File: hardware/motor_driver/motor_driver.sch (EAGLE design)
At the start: 79 parts

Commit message: Added temperature sensor
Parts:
- added C27: 2.2u, adafruit:C-USC0805
- added R32: 10K, adafruit:R-US_M0805
- added TEMP: 22-23-2021, con-molex:22-23-2021
- added U$11: NCP18XH103F03RB, bldc_lib:NCP18XH103F03RB
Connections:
- new net TEMP: C27.1, R32.1, TEMP-2.S, U$11.1
- net +3V3: now also U$11.2
- net DGND: now also C27.2, R32.2, TEMP-1.S
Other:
- note added: "NTC 10K"
- note added: "Temperature Sensor"
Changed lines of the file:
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@@
 <setting verticaltext="up"/>
 </settings>
-<grid distance="0.1" unitdist="inch" unit="inch" style="lines" multiple="1" display="yes" altdistance="0.01" altunitdist="inch" altunit="inch"/>
+<grid distance="0.1" unitdist="inch" unit="inch" style="lines" multiple="1" display="no" altdistance="0.01" altunitdist="inch" altunit="inch"/>
 <layers>
 <layer number="1" name="Top" color="4" fill="1" visible="no" active="no"/>
@@
 <part name="PT1" library="SparkFun-Passives" deviceset="2PT_GND_TIE" device=""/>
 <part name="PT2" library="SparkFun-Passives" deviceset="2PT_GND_TIE" device=""/>
+<part name="U$11" library="bldc_lib" deviceset="NCP18XH103F03RB" device=""/>
+<part name="R32" library="adafruit" deviceset="R-US_" device="M0805" value="10K"/>
+<part name="SUPPLY24" library="supply2" deviceset="DGND" device=""/>
+<part name="+3V2" library="supply1" deviceset="+3V3" device=""/>
+<part name="C27" library="adafruit" deviceset="C-US" device="C0805" value="2.2u"/>
+<part name="TEMP" library="con-molex" deviceset="22-23-2021" device=""/>
 </parts>
 <sheets>
@@
 <wire x1="88.9" y1="-66.04" x2="124.46" y2="-66.04" width="0.1524" layer="97" style="shortdash"/>
 <text x="96.52" y="-63.5" size="2.54" layer="97">Connect Grounds</text>
+<text x="7.62" y="-50.8" size="1.778" layer="97">NTC 10K</text>
+<wire x1="55.88" y1="-22.86" x2="55.88" y2="-53.34" width="0.1524" layer="97" style="shortdash"/>
+<wire x1="55.88" y1="-53.34" x2="-5.08" y2="-53.34" width="0.1524" layer="97" style="shortdash"/>
+<wire x1="-5.08" y1="-53.34" x2="-5.08" y2="-22.86" width="0.1524" layer="97" style="shortdash"/>
+<wire x1="-5.08" y1="-22.86" x2="55.88" y2="-22.86" width="0.1524" layer="97" style="shortdash"/>
+<text x="30.48" y="-50.8" size="1.778" layer="97">Temperature Sensor</text>
 </plain>
 <instances>
@@
 <instance part="PT1" gate="G$1" x="99.06" y="-86.36"/>
 <instance part="PT2" gate="G$1" x="114.3" y="-86.36"/>
+<instance part="U$11" gate="G$1" x="10.16" y="-40.64"/>
+<instance part="R32" gate="G$1" x="25.4" y="-40.64"/>
+<instance part="SUPPLY24" gate="G$1" x="33.02" y="-40.64" rot="R90"/>
+<instance part="+3V2" gate="G$1" x="0" y="-40.64" rot="R90"/>
+<instance part="C27" gate="G$1" x="22.86" y="-33.02" rot="R90"/>
+<instance part="TEMP" gate="-1" x="45.72" y="-35.56" rot="R270"/>
+<instance part="TEMP" gate="-2" x="43.18" y="-35.56" rot="R270"/>
 </instances>
 <busses>
@@
 <label x="104.14" y="-83.82" size="2.54" layer="95" rot="R90" xref="yes"/>
 </segment>
+<segment>
+<pinref part="R32" gate="G$1" pin="2"/>
+<pinref part="SUPPLY24" gate="G$1" pin="DGND"/>
+<pinref part="C27" gate="G$1" pin="2"/>
+<wire x1="27.94" y1="-33.02" x2="30.48" y2="-33.02" width="0.1524" layer="91"/>
+<wire x1="30.48" y1="-33.02" x2="30.48" y2="-40.64" width="0.1524" layer="91"/>
+<junction x="30.48" y="-40.64"/>
+</segment>
+<segment>
+<pinref part="TEMP" gate="-1" pin="S"/>
+<wire x1="45.72" y1="-33.02" x2="45.72" y2="-30.48" width="0.1524" layer="91"/>
+<label x="45.72" y="-30.48" size="1.016" layer="95" rot="R90" xref="yes"/>
+</segment>
 </net>
 <net name="+5V" class="0">
@@
 <junction x="99.06" y="-33.02"/>
 </segment>
-</net>
+<segment>
+<pinref part="+3V2" gate="G$1" pin="+3V3"/>
+<pinref part="U$11" gate="G$1" pin="2"/>
+<wire x1="2.54" y1="-40.64" x2="5.08" y2="-40.64" width="0.1524" layer="91"/>
+</segment>
+</net>
+<net name="TEMP" class="0">
+<segment>
+<pinref part="U$11" gate="G$1" pin="1"/>
+<pinref part="R32" gate="G$1" pin="1"/>
+<wire x1="15.24" y1="-40.64" x2="17.78" y2="-40.64" width="0.1524" layer="91"/>
+<pinref part="C27" gate="G$1" pin="1"/>
+<wire x1="17.78" y1="-40.64" x2="20.32" y2="-40.64" width="0.1524" layer="91"/>
+<wire x1="20.32" y1="-33.02" x2="17.78" y2="-33.02" width="0.1524" layer="91"/>
+<wire x1="17.78" y1="-33.02" x2="17.78" y2="-40.64" width="0.1524" layer="91"/>
+<junction x="17.78" y="-40.64"/>
+<label x="17.78" y="-33.02" size="1.778" layer="95" rot="R90" xref="yes"/>
+</segment>
+<segment>
+<pinref part="TEMP" gate="-2" pin="S"/>
+<wire x1="43.18" y1="-33.02" x2="43.18" y2="-30.48" width="0.1524" layer="91"/>
+<label x="43.18" y="-30.48" size="1.016" layer="95" rot="R90" xref="yes"/>
+</segment>
+</net>

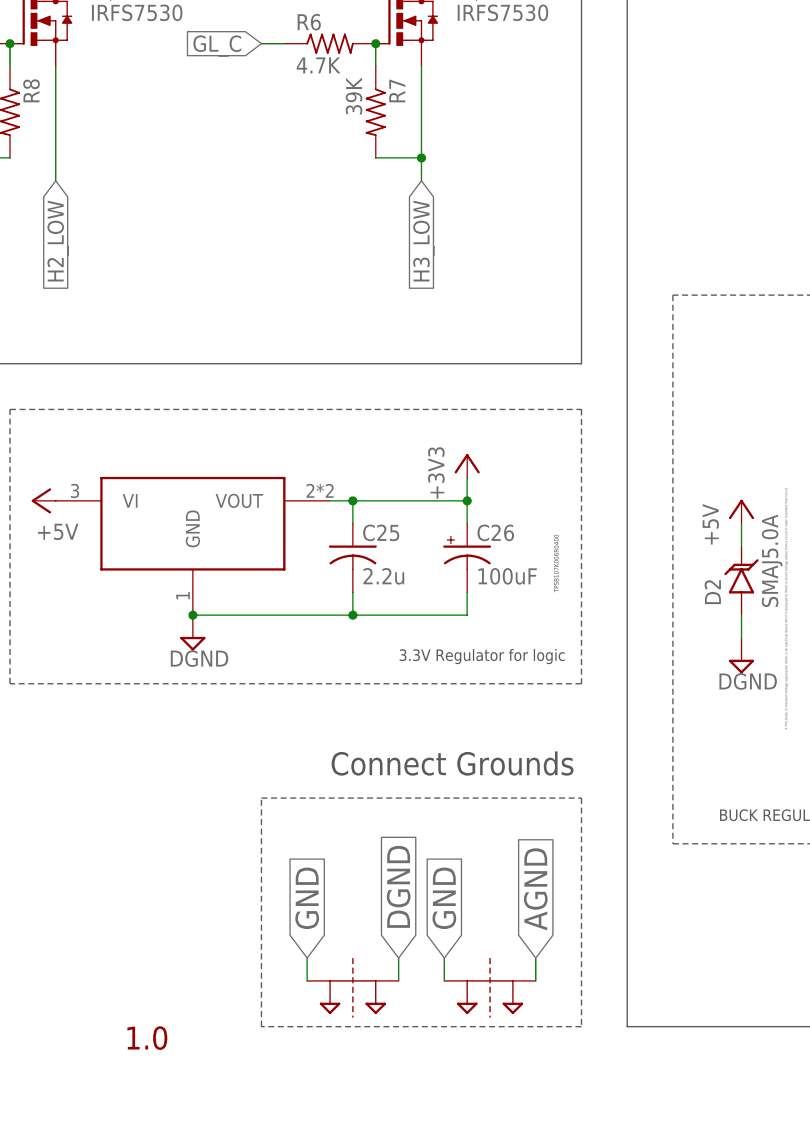
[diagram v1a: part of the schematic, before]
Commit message: Added connectors for motor and power
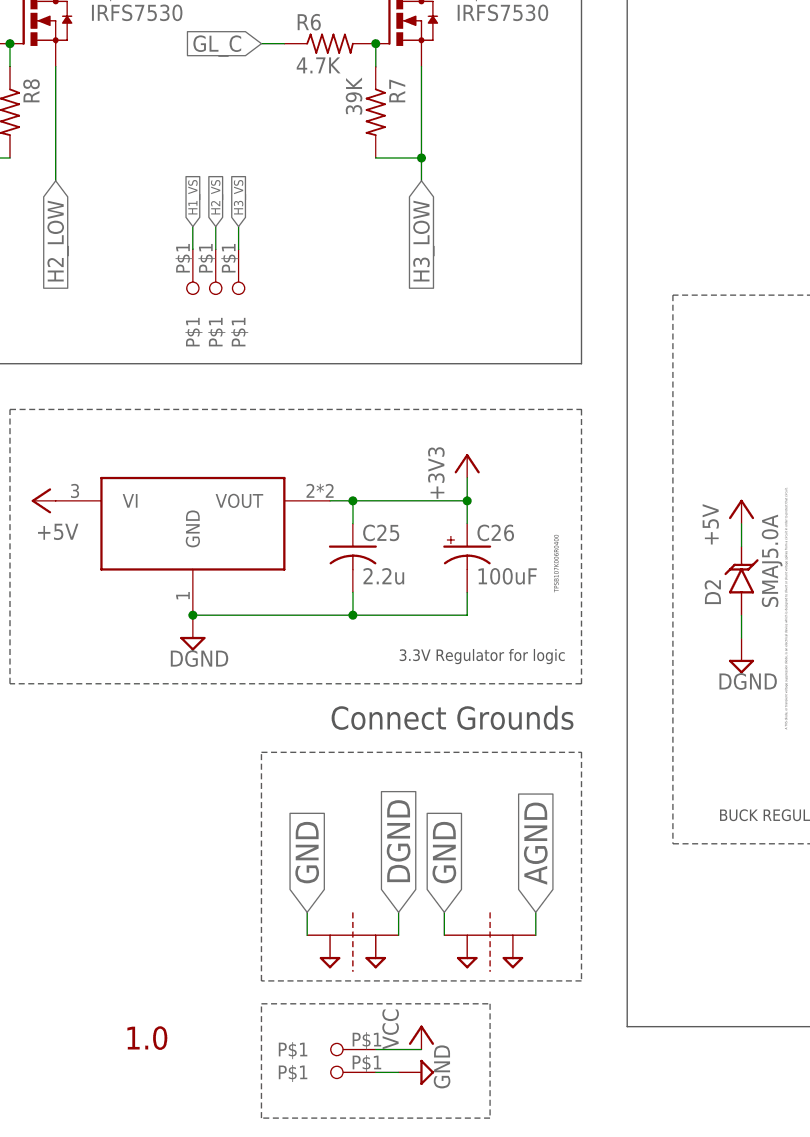
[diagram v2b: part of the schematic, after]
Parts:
- added U$12, U$13, U$14, U$15, U$16: 1CONN_SOLDER, bldc_lib:1CONN_SOLDER
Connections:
- net GND: now also U$16.P$1
- net H1_VS: now also U$14.P$1
- net H2_VS: now also U$13.P$1
- net H3_VS: now also U$12.P$1
- net VCC: now also U$15.P$1
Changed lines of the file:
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@@
 <part name="C27" library="adafruit" deviceset="C-US" device="C0805" value="2.2u"/>
 <part name="TEMP" library="con-molex" deviceset="22-23-2021" device=""/>
+<part name="U$12" library="bldc_lib" deviceset="1CONN_SOLDER" device=""/>
+<part name="U$13" library="bldc_lib" deviceset="1CONN_SOLDER" device=""/>
+<part name="U$14" library="bldc_lib" deviceset="1CONN_SOLDER" device=""/>
+<part name="U$15" library="bldc_lib" deviceset="1CONN_SOLDER" device=""/>
+<part name="U$16" library="bldc_lib" deviceset="1CONN_SOLDER" device=""/>
+<part name="P+14" library="supply1" deviceset="VCC" device=""/>
+<part name="SUPPLY25" library="supply2" deviceset="GND" device=""/>
 </parts>
 <sheets>
@@
 <text x="27.94" y="-83.82" size="2.54" layer="94">Motor Driver (2015)</text>
 <text x="73.66" y="-93.98" size="2.54" layer="94">1.0</text>
-<wire x1="124.46" y1="-66.04" x2="124.46" y2="-91.44" width="0.1524" layer="97" style="shortdash"/>
-<wire x1="124.46" y1="-91.44" x2="88.9" y2="-91.44" width="0.1524" layer="97" style="shortdash"/>
-<wire x1="88.9" y1="-91.44" x2="88.9" y2="-66.04" width="0.1524" layer="97" style="shortdash"/>
-<wire x1="88.9" y1="-66.04" x2="124.46" y2="-66.04" width="0.1524" layer="97" style="shortdash"/>
-<text x="96.52" y="-63.5" size="2.54" layer="97">Connect Grounds</text>
+<wire x1="124.46" y1="-60.96" x2="124.46" y2="-86.36" width="0.1524" layer="97" style="shortdash"/>
+<wire x1="124.46" y1="-86.36" x2="88.9" y2="-86.36" width="0.1524" layer="97" style="shortdash"/>
+<wire x1="88.9" y1="-86.36" x2="88.9" y2="-60.96" width="0.1524" layer="97" style="shortdash"/>
+<wire x1="88.9" y1="-60.96" x2="124.46" y2="-60.96" width="0.1524" layer="97" style="shortdash"/>
+<text x="96.52" y="-58.42" size="2.54" layer="97">Connect Grounds</text>
 <text x="7.62" y="-50.8" size="1.778" layer="97">NTC 10K</text>
 <wire x1="55.88" y1="-22.86" x2="55.88" y2="-53.34" width="0.1524" layer="97" style="shortdash"/>
@@
 <wire x1="-5.08" y1="-22.86" x2="55.88" y2="-22.86" width="0.1524" layer="97" style="shortdash"/>
 <text x="30.48" y="-50.8" size="1.778" layer="97">Temperature Sensor</text>
+<wire x1="88.9" y1="-88.9" x2="114.3" y2="-88.9" width="0.1524" layer="97" style="shortdash"/>
+<wire x1="114.3" y1="-88.9" x2="114.3" y2="-101.6" width="0.1524" layer="97" style="shortdash"/>
+<wire x1="114.3" y1="-101.6" x2="88.9" y2="-101.6" width="0.1524" layer="97" style="shortdash"/>
+<wire x1="88.9" y1="-101.6" x2="88.9" y2="-88.9" width="0.1524" layer="97" style="shortdash"/>
 </plain>
 <instances>
@@
 <instance part="FRAME1" gate="G$1" x="-15.24" y="-101.6"/>
 <instance part="P+1" gate="VCC" x="66.04" y="53.34"/>
-<instance part="PT1" gate="G$1" x="99.06" y="-86.36"/>
-<instance part="PT2" gate="G$1" x="114.3" y="-86.36"/>
+<instance part="PT1" gate="G$1" x="99.06" y="-81.28"/>
+<instance part="PT2" gate="G$1" x="114.3" y="-81.28"/>
 <instance part="U$11" gate="G$1" x="10.16" y="-40.64"/>
 <instance part="R32" gate="G$1" x="25.4" y="-40.64"/>
@@
 <instance part="TEMP" gate="-1" x="45.72" y="-35.56" rot="R270"/>
 <instance part="TEMP" gate="-2" x="43.18" y="-35.56" rot="R270"/>
+<instance part="U$12" gate="G$1" x="86.36" y="-7.62" rot="R270"/>
+<instance part="U$13" gate="G$1" x="83.82" y="-7.62" rot="R270"/>
+<instance part="U$14" gate="G$1" x="81.28" y="-7.62" rot="R270"/>
+<instance part="U$15" gate="G$1" x="99.06" y="-93.98" rot="R180"/>
+<instance part="U$16" gate="G$1" x="99.06" y="-96.52" rot="R180"/>
+<instance part="P+14" gate="VCC" x="106.68" y="-91.44"/>
+<instance part="SUPPLY25" gate="GND" x="106.68" y="-96.52" rot="R90"/>
 </instances>
 <busses>
@@
 <label x="327.66" y="-33.02" size="1.016" layer="95" rot="R180" xref="yes"/>
 </segment>
+<segment>
+<pinref part="U$14" gate="G$1" pin="P$1"/>
+<wire x1="81.28" y1="-5.08" x2="81.28" y2="-2.54" width="0.1524" layer="91"/>
+<label x="81.28" y="-2.54" size="1.016" layer="95" rot="R90" xref="yes"/>
+</segment>
 </net>
 <net name="H2_VS" class="0">
@@
 <label x="327.66" y="-50.8" size="1.016" layer="95" rot="R180" xref="yes"/>
 </segment>
+<segment>
+<pinref part="U$13" gate="G$1" pin="P$1"/>
+<wire x1="83.82" y1="-5.08" x2="83.82" y2="-2.54" width="0.1524" layer="91"/>
+<label x="83.82" y="-2.54" size="1.016" layer="95" rot="R90" xref="yes"/>
+</segment>
 </net>
 <net name="H3_VS" class="0">
@@
 <wire x1="330.2" y1="-68.58" x2="327.66" y2="-68.58" width="0.1524" layer="91"/>
 <label x="327.66" y="-68.58" size="1.016" layer="95" rot="R180" xref="yes"/>
+</segment>
+<segment>
+<pinref part="U$12" gate="G$1" pin="P$1"/>
+<wire x1="86.36" y1="-5.08" x2="86.36" y2="-2.54" width="0.1524" layer="91"/>
+<label x="86.36" y="-2.54" size="1.016" layer="95" rot="R90" xref="yes"/>
 </segment>
 </net>
@@
 </segment>
 <segment>
-<wire x1="93.98" y1="-86.36" x2="93.98" y2="-83.82" width="0.1524" layer="91"/>
-<label x="93.98" y="-83.82" size="2.54" layer="95" rot="R90" xref="yes"/>
+<wire x1="93.98" y1="-81.28" x2="93.98" y2="-78.74" width="0.1524" layer="91"/>
+<label x="93.98" y="-78.74" size="2.54" layer="95" rot="R90" xref="yes"/>
 <pinref part="PT1" gate="G$1" pin="P$1"/>
 </segment>
 <segment>
 <pinref part="PT2" gate="G$1" pin="P$1"/>
-<wire x1="109.22" y1="-86.36" x2="109.22" y2="-83.82" width="0.1524" layer="91"/>
-<label x="109.22" y="-83.82" size="2.54" layer="95" rot="R90" xref="yes"/>
+<wire x1="109.22" y1="-81.28" x2="109.22" y2="-78.74" width="0.1524" layer="91"/>
+<label x="109.22" y="-78.74" size="2.54" layer="95" rot="R90" xref="yes"/>
+</segment>
+<segment>
+<pinref part="U$16" gate="G$1" pin="P$1"/>
+<wire x1="101.6" y1="-96.52" x2="104.14" y2="-96.52" width="0.1524" layer="91"/>
+<pinref part="SUPPLY25" gate="GND" pin="GND"/>
 </segment>
 </net>
@@
 <segment>
 <pinref part="PT2" gate="G$1" pin="P$2"/>
-<wire x1="119.38" y1="-86.36" x2="119.38" y2="-83.82" width="0.1524" layer="91"/>
-<label x="119.38" y="-83.82" size="2.54" layer="95" rot="R90" xref="yes"/>
+<wire x1="119.38" y1="-81.28" x2="119.38" y2="-78.74" width="0.1524" layer="91"/>
+<label x="119.38" y="-78.74" size="2.54" layer="95" rot="R90" xref="yes"/>
 </segment>
 </net>
@@
 <segment>
 <pinref part="PT1" gate="G$1" pin="P$2"/>
-<wire x1="104.14" y1="-86.36" x2="104.14" y2="-83.82" width="0.1524" layer="91"/>
-<label x="104.14" y="-83.82" size="2.54" layer="95" rot="R90" xref="yes"/>
+<wire x1="104.14" y1="-81.28" x2="104.14" y2="-78.74" width="0.1524" layer="91"/>
+<label x="104.14" y="-78.74" size="2.54" layer="95" rot="R90" xref="yes"/>
 </segment>
 <segment>
@@
 <wire x1="66.04" y1="48.26" x2="66.04" y2="50.8" width="0.1524" layer="91"/>
 </segment>
-</net>
+<segment>
+<pinref part="U$15" gate="G$1" pin="P$1"/>
+<wire x1="101.6" y1="-93.98" x2="106.68" y2="-93.98" width="0.1524" layer="91"/>
+<pinref part="P+14" gate="VCC" pin="VCC"/>
+</segment>
+</net>

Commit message: Grounded MOSFETS
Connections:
- removed net H2_LOW: U$3.S, U$7.SL_B
- removed net N$25: R10.2, U$8.2
- removed net N$9: R12.2, U$9.2
- net GND: now also U$3.S, U$7.SL_B
- net H1_LOW: now also R10.2, U$8.2
- net H3_LOW: now also R12.2, U$9.2
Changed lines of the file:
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@@
 <part name="P+14" library="supply1" deviceset="VCC" device=""/>
 <part name="SUPPLY25" library="supply2" deviceset="GND" device=""/>
+<part name="SUPPLY26" library="supply2" deviceset="GND" device=""/>
+<part name="SUPPLY27" library="supply2" deviceset="GND" device=""/>
 </parts>
 <sheets>
@@
 <text x="58.42" y="63.5" size="1.778" layer="97">MOSFET</text>
 <wire x1="238.76" y1="-50.8" x2="238.76" y2="-86.36" width="0.1524" layer="97" style="shortdash"/>
-<wire x1="238.76" y1="-86.36" x2="299.72" y2="-86.36" width="0.1524" layer="97" style="shortdash"/>
-<wire x1="299.72" y1="-86.36" x2="299.72" y2="-25.4" width="0.1524" layer="97" style="shortdash"/>
-<wire x1="299.72" y1="-25.4" x2="276.86" y2="-25.4" width="0.1524" layer="97" style="shortdash"/>
+<wire x1="238.76" y1="-86.36" x2="314.96" y2="-86.36" width="0.1524" layer="97" style="shortdash"/>
+<wire x1="314.96" y1="-86.36" x2="314.96" y2="-25.4" width="0.1524" layer="97" style="shortdash"/>
+<wire x1="314.96" y1="-25.4" x2="276.86" y2="-25.4" width="0.1524" layer="97" style="shortdash"/>
 <wire x1="276.86" y1="-25.4" x2="276.86" y2="-27.94" width="0.1524" layer="97" style="shortdash"/>
 <wire x1="276.86" y1="-27.94" x2="243.84" y2="-27.94" width="0.1524" layer="97" style="shortdash"/>
@@
 <instance part="P+14" gate="VCC" x="106.68" y="-91.44"/>
 <instance part="SUPPLY25" gate="GND" x="106.68" y="-96.52" rot="R90"/>
+<instance part="SUPPLY26" gate="GND" x="66.04" y="7.62"/>
+<instance part="SUPPLY27" gate="GND" x="269.24" y="-12.7" rot="R90"/>
 </instances>
 <busses>
@@
 <label x="264.16" y="0" size="1.016" layer="95" xref="yes"/>
 </segment>
-</net>
-<net name="H2_LOW" class="0">
-<segment>
-<pinref part="U$3" gate="G$1" pin="S"/>
-<wire x1="66.04" y1="15.24" x2="66.04" y2="2.54" width="0.1524" layer="91"/>
-<label x="66.04" y="2.54" size="1.778" layer="95" rot="R270" xref="yes"/>
-</segment>
-<segment>
-<pinref part="U$7" gate="G$1" pin="SL_B"/>
-<wire x1="261.62" y1="-12.7" x2="264.16" y2="-12.7" width="0.1524" layer="91"/>
-<label x="264.16" y="-12.7" size="1.016" layer="95" xref="yes"/>
+<segment>
+<pinref part="R10" gate="G$1" pin="2"/>
+<pinref part="U$8" gate="R$1" pin="2"/>
+<wire x1="292.1" y1="-30.48" x2="294.64" y2="-30.48" width="0.1524" layer="91"/>
+<wire x1="294.64" y1="-30.48" x2="299.72" y2="-30.48" width="0.1524" layer="91"/>
+<junction x="294.64" y="-30.48"/>
+<label x="299.72" y="-30.48" size="1.778" layer="95" xref="yes"/>
 </segment>
 </net>
@@
 <label x="264.16" y="-25.4" size="1.016" layer="95" xref="yes"/>
 </segment>
+<segment>
+<pinref part="U$9" gate="R$1" pin="2"/>
+<pinref part="R12" gate="G$1" pin="2"/>
+<wire x1="294.64" y1="-50.8" x2="292.1" y2="-50.8" width="0.1524" layer="91"/>
+<wire x1="294.64" y1="-50.8" x2="299.72" y2="-50.8" width="0.1524" layer="91"/>
+<junction x="294.64" y="-50.8"/>
+<label x="299.72" y="-50.8" size="1.778" layer="95" xref="yes"/>
+</segment>
 </net>
 <net name="GL_A" class="0">
@@
 <pinref part="C3" gate="G$1" pin="1"/>
 <wire x1="274.32" y1="-15.24" x2="261.62" y2="-15.24" width="0.1524" layer="91"/>
-</segment>
-</net>
-<net name="N$9" class="0">
-<segment>
-<pinref part="U$9" gate="R$1" pin="2"/>
-<pinref part="R12" gate="G$1" pin="2"/>
-<wire x1="294.64" y1="-50.8" x2="292.1" y2="-50.8" width="0.1524" layer="91"/>
 </segment>
 </net>
@@
 <wire x1="271.78" y1="-40.64" x2="276.86" y2="-40.64" width="0.1524" layer="91"/>
 <junction x="276.86" y="-40.64"/>
-</segment>
-</net>
-<net name="N$25" class="0">
-<segment>
-<pinref part="R10" gate="G$1" pin="2"/>
-<pinref part="U$8" gate="R$1" pin="2"/>
-<wire x1="292.1" y1="-30.48" x2="294.64" y2="-30.48" width="0.1524" layer="91"/>
 </segment>
 </net>
@@
 <pinref part="SUPPLY25" gate="GND" pin="GND"/>
 </segment>
-</net>
+<segment>
+<pinref part="U$3" gate="G$1" pin="S"/>
+<wire x1="66.04" y1="15.24" x2="66.04" y2="10.16" width="0.1524" layer="91"/>
+<pinref part="SUPPLY26" gate="GND" pin="GND"/>
+</segment>
+<segment>
+<pinref part="U$7" gate="G$1" pin="SL_B"/>
+<wire x1="261.62" y1="-12.7" x2="266.7" y2="-12.7" width="0.1524" layer="91"/>
+<pinref part="SUPPLY27" gate="GND" pin="GND"/>
+</segment>
+</net>

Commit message: Made the changes mike suggested
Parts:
- R19: value 10M -> 1M
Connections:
- net DGND: now also C11.1
- net GND: no longer C11.1
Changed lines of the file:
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@@
 <part name="R18" library="adafruit" deviceset="R-US_" device="R0603" value="10K"/>
 <part name="SUPPLY7" library="supply2" deviceset="DGND" device=""/>
-<part name="R19" library="adafruit" deviceset="R-US_" device="R0603" value="10M"/>
+<part name="R19" library="adafruit" deviceset="R-US_" device="R0603" value="1M"/>
 <part name="SUPPLY8" library="supply2" deviceset="DGND" device=""/>
 <part name="R20" library="adafruit" deviceset="R-US_" device="R0603" value="15K"/>
@@
 <part name="P+8" library="supply1" deviceset="+5V" device=""/>
 <part name="C11" library="SparkFun-Passives" deviceset="CAP" device="1206" value="10u,50V"/>
-<part name="SUPPLY13" library="supply2" deviceset="GND" device=""/>
 <part name="P+9" library="supply1" deviceset="VCC" device=""/>
 <part name="CTRL" library="con-molex" deviceset="22-23-2041" device=""/>
@@
 <part name="SUPPLY26" library="supply2" deviceset="GND" device=""/>
 <part name="SUPPLY27" library="supply2" deviceset="GND" device=""/>
+<part name="SUPPLY13" library="supply2" deviceset="DGND" device=""/>
 </parts>
 <sheets>
@@
 <instance part="P+8" gate="1" x="142.24" y="-33.02"/>
 <instance part="C11" gate="G$1" x="208.28" y="-20.32" rot="R90"/>
-<instance part="SUPPLY13" gate="GND" x="200.66" y="-17.78" rot="R180"/>
 <instance part="P+9" gate="VCC" x="218.44" y="-15.24"/>
 <instance part="CTRL" gate="-1" x="200.66" y="43.18" rot="R270"/>
@@
 <instance part="SUPPLY26" gate="GND" x="66.04" y="7.62"/>
 <instance part="SUPPLY27" gate="GND" x="269.24" y="-12.7" rot="R90"/>
+<instance part="SUPPLY13" gate="G$1" x="200.66" y="-17.78" rot="R180"/>
 </instances>
 <busses>
@@
 <pinref part="SUPPLY2" gate="GND" pin="GND"/>
 <junction x="294.64" y="-60.96"/>
-</segment>
-<segment>
-<pinref part="SUPPLY13" gate="GND" pin="GND"/>
-<pinref part="C11" gate="G$1" pin="1"/>
-<wire x1="200.66" y1="-20.32" x2="203.2" y2="-20.32" width="0.1524" layer="91"/>
 </segment>
 <segment>
@@
 <label x="45.72" y="-30.48" size="1.016" layer="95" rot="R90" xref="yes"/>
 </segment>
-</net>
+<segment>
+<pinref part="C11" gate="G$1" pin="1"/>
+<wire x1="200.66" y1="-20.32" x2="203.2" y2="-20.32" width="0.1524" layer="91"/>
+<pinref part="SUPPLY13" gate="G$1" pin="DGND"/>
+</segment>
+</net>
